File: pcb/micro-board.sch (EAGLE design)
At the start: 122 parts, among them IC1 STM32F401RET6U, IC2 LDS3985M33R, IC3 LDS3985M33R, IC4 HX711, IC5 TLV2462IP, J12 B2B-PH-K-S_LF__SN_, J14 3V3 LED, J15 VDDA LED, J16 HX711 LED, J18 DC Power, J3 Button / ADC Header, Q1 S8550, U1 MCP73831.SOT23-5, U2 BR24S64FJ-WE2, X1 16MHz

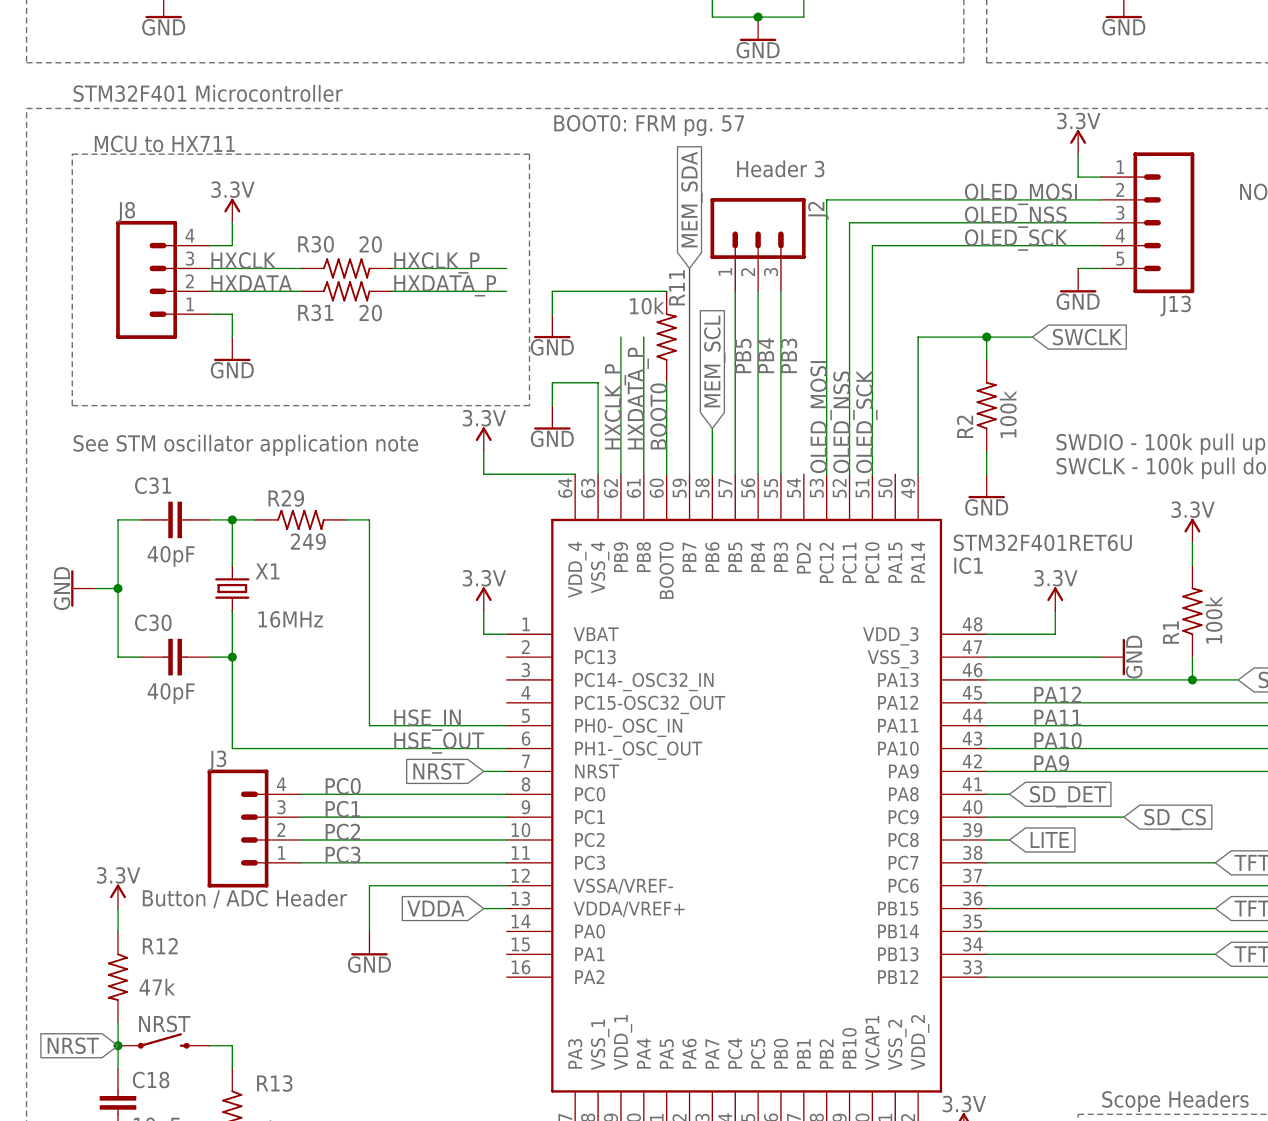
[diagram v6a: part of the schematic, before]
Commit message: Updated the PCB with more silkscreen and ESD protection resistors
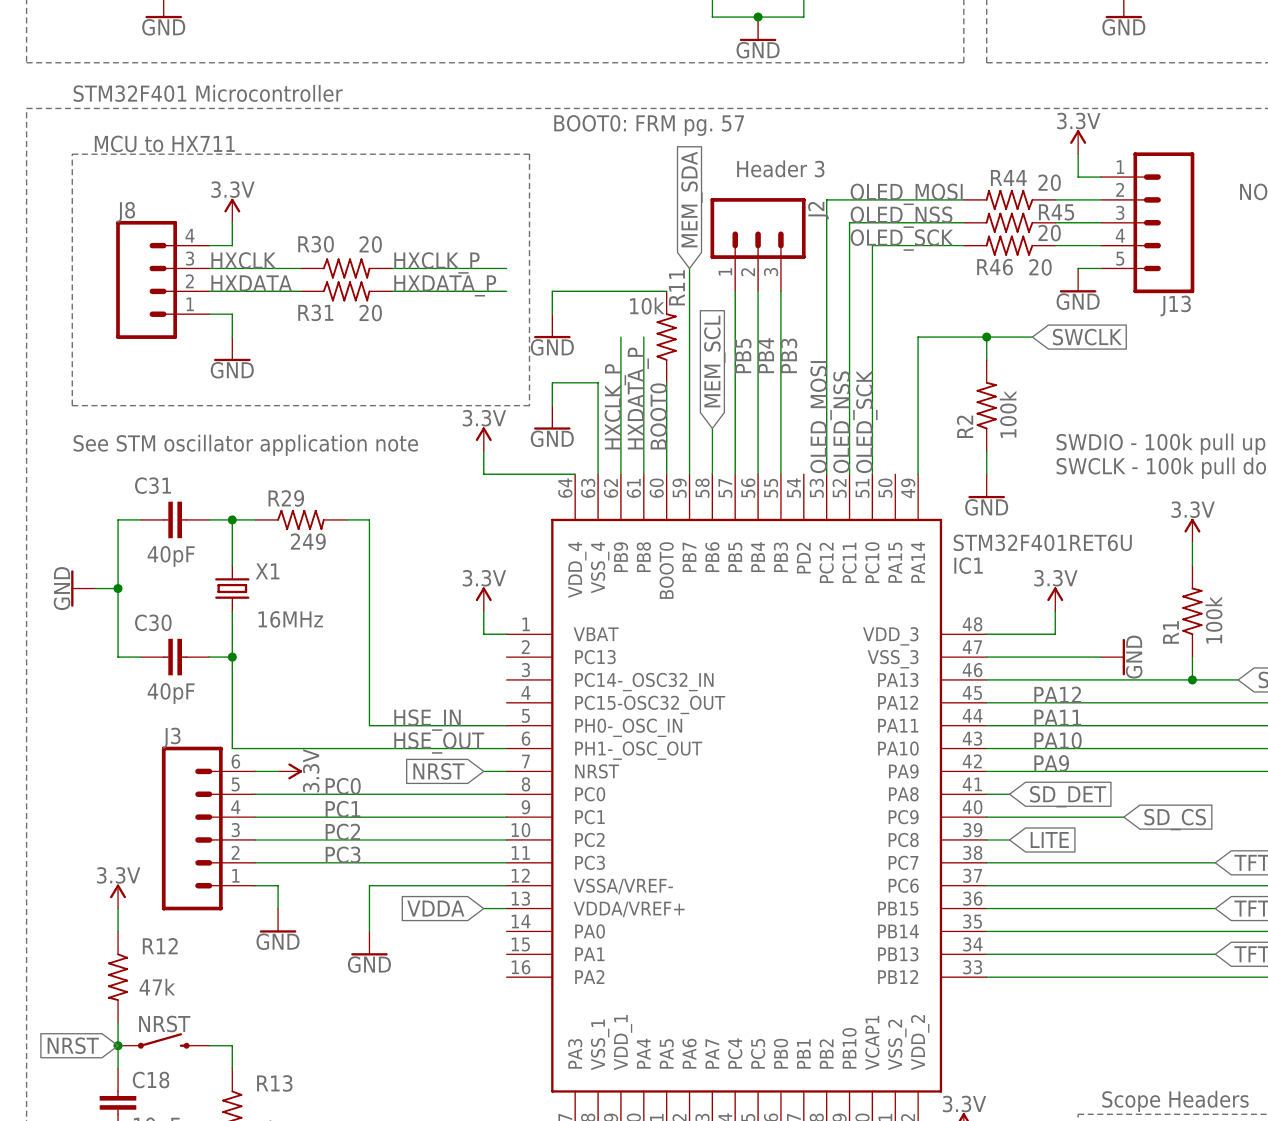
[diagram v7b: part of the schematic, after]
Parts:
- added R44, R45, R46: 20, LinnesLab-Passives:RESISTOR0603
- J3: value Button / ADC Header -> (none); device LinnesLab-Connectors:CONN_04 -> LinnesLab-Connectors:CONN_06LOCK
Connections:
- new net N$20: J13.3, R45.1
- new net N$21: J13.4, R46.1
- new net N$8: J13.2, R44.1
- net 3.3V: now also J3.6
- net GND: now also J3.1
- net OLED_MOSI: now also R44.2; no longer J13.2
- net OLED_NSS: now also R45.2; no longer J13.3
- net OLED_SCK: now also R46.2; no longer J13.4
- net PC0: now also J3.5; no longer J3.4
- net PC1: now also J3.4; no longer J3.3
- net PC2: now also J3.3; no longer J3.2
- net PC3: now also J3.2; no longer J3.1
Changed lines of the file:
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@@
 <setting verticaltext="up"/>
 </settings>
-<grid distance="0.1" unitdist="inch" unit="inch" style="lines" multiple="1" display="yes" altdistance="0.01" altunitdist="inch" altunit="inch"/>
+<grid distance="0.1" unitdist="inch" unit="inch" style="lines" multiple="1" display="no" altdistance="0.01" altunitdist="inch" altunit="inch"/>
 <layers>
 <layer number="1" name="Top" color="4" fill="1" visible="no" active="no"/>
@@
 <part name="GND13" library="LinnesLab-Symbols" deviceset="GND" device=""/>
 <part name="J2" library="LinnesLab-Connectors" deviceset="CONN_03" device=""/>
-<part name="J3" library="LinnesLab-Connectors" deviceset="CONN_04" device="" value="Button / ADC Header"/>
 <part name="GND14" library="LinnesLab-Symbols" deviceset="GND" device=""/>
 <part name="R1" library="LinnesLab-Passives" deviceset="RESISTOR" device="0603" package3d_urn="urn:adsk.eagle:package:15661944/2" value="100k"/>
@@
 <part name="R42" library="LinnesLab-Passives" deviceset="RESISTOR" device="0603" package3d_urn="urn:adsk.eagle:package:15661944/2" value="20"/>
 <part name="R43" library="LinnesLab-Passives" deviceset="RESISTOR" device="0603" package3d_urn="urn:adsk.eagle:package:15661944/2" value="20"/>
+<part name="R44" library="LinnesLab-Passives" deviceset="RESISTOR" device="0603" package3d_urn="urn:adsk.eagle:package:15661944/2" value="20"/>
+<part name="R45" library="LinnesLab-Passives" deviceset="RESISTOR" device="0603" package3d_urn="urn:adsk.eagle:package:15661944/2" value="20"/>
+<part name="R46" library="LinnesLab-Passives" deviceset="RESISTOR" device="0603" package3d_urn="urn:adsk.eagle:package:15661944/2" value="20"/>
+<part name="J3" library="LinnesLab-Connectors" deviceset="CONN_06" device="LOCK"/>
+<part name="GND18" library="LinnesLab-Symbols" deviceset="GND" device=""/>
+<part name="SUPPLY41" library="LinnesLab-Symbols" deviceset="3.3V" device=""/>
 </parts>
 <sheets>
@@
 <attribute name="NAME" x="86.868" y="149.86" size="1.778" layer="95" font="vector" rot="R270"/>
 </instance>
-<instance part="J3" gate="G$1" x="25.4" y="78.74" smashed="yes">
-<attribute name="VALUE" x="12.7" y="71.374" size="1.778" layer="96" font="vector"/>
-<attribute name="NAME" x="20.32" y="86.868" size="1.778" layer="95" font="vector"/>
-</instance>
 <instance part="GND14" gate="G$1" x="58.42" y="124.46" smashed="yes">
 <attribute name="VALUE" x="58.42" y="124.206" size="1.778" layer="96" align="top-center"/>
@@
 <attribute name="VALUE" x="75.946" y="30.734" size="1.778" layer="96" rot="R90"/>
 </instance>
+<instance part="R44" gate="G$1" x="109.22" y="149.86" smashed="yes" rot="R180">
+<attribute name="NAME" x="111.252" y="153.1874" size="1.778" layer="95" rot="R180"/>
+<attribute name="VALUE" x="115.062" y="152.654" size="1.778" layer="96" rot="R180"/>
+</instance>
+<instance part="R45" gate="G$1" x="109.22" y="147.32" smashed="yes" rot="R180">
+<attribute name="NAME" x="116.586" y="149.3774" size="1.778" layer="95" rot="R180"/>
+<attribute name="VALUE" x="115.062" y="147.066" size="1.778" layer="96" rot="R180"/>
+</instance>
+<instance part="R46" gate="G$1" x="109.22" y="144.78" smashed="yes" rot="R180">
+<attribute name="NAME" x="109.728" y="143.2814" size="1.778" layer="95" rot="R180"/>
+<attribute name="VALUE" x="114.046" y="143.256" size="1.778" layer="96" rot="R180"/>
+</instance>
+<instance part="J3" gate="G$1" x="20.32" y="78.74" smashed="yes">
+<attribute name="VALUE" x="15.24" y="68.834" size="1.778" layer="96" font="vector"/>
+<attribute name="NAME" x="15.24" y="89.408" size="1.778" layer="95" font="vector"/>
+</instance>
+<instance part="GND18" gate="G$1" x="27.94" y="68.58" smashed="yes">
+<attribute name="VALUE" x="27.94" y="68.326" size="1.778" layer="96" align="top-center"/>
+</instance>
+<instance part="SUPPLY41" gate="G$1" x="27.94" y="86.36" smashed="yes" rot="R270">
+<attribute name="VALUE" x="30.734" y="86.36" size="1.778" layer="96" rot="R270" align="bottom-center"/>
+</instance>
 </instances>
 <busses>
@@
 <wire x1="182.88" y1="127" x2="187.96" y2="127" width="0.1524" layer="91"/>
 </segment>
+<segment>
+<pinref part="GND18" gate="G$1" pin="GND"/>
+<pinref part="J3" gate="G$1" pin="1"/>
+<wire x1="27.94" y1="71.12" x2="27.94" y2="73.66" width="0.1524" layer="91"/>
+<wire x1="27.94" y1="73.66" x2="25.4" y2="73.66" width="0.1524" layer="91"/>
+</segment>
 </net>
 <net name="N$3" class="0">
@@
 <segment>
 <pinref part="IC1" gate="G$1" pin="PC3"/>
-<pinref part="J3" gate="G$1" pin="1"/>
-<wire x1="53.34" y1="76.2" x2="30.48" y2="76.2" width="0.1524" layer="91"/>
+<wire x1="53.34" y1="76.2" x2="25.4" y2="76.2" width="0.1524" layer="91"/>
 <label x="33.02" y="76.2" size="1.778" layer="95"/>
+<pinref part="J3" gate="G$1" pin="2"/>
 </segment>
 </net>
@@
 <segment>
 <pinref part="IC1" gate="G$1" pin="PC10"/>
-<pinref part="J13" gate="G$1" pin="4"/>
 <wire x1="93.98" y1="119.38" x2="93.98" y2="144.78" width="0.1524" layer="91"/>
-<wire x1="93.98" y1="144.78" x2="119.38" y2="144.78" width="0.1524" layer="91"/>
-<label x="104.14" y="144.78" size="1.778" layer="95"/>
+<label x="91.44" y="144.78" size="1.778" layer="95"/>
 <label x="93.98" y="119.38" size="1.778" layer="95" rot="R90"/>
+<pinref part="R46" gate="G$1" pin="2"/>
+<wire x1="93.98" y1="144.78" x2="104.14" y2="144.78" width="0.1524" layer="91"/>
 </segment>
 </net>
@@
 <pinref part="IC1" gate="G$1" pin="PC11"/>
 <wire x1="91.44" y1="119.38" x2="91.44" y2="147.32" width="0.1524" layer="91"/>
-<pinref part="J13" gate="G$1" pin="3"/>
-<wire x1="91.44" y1="147.32" x2="119.38" y2="147.32" width="0.1524" layer="91"/>
-<label x="104.14" y="147.32" size="1.778" layer="95"/>
+<label x="91.44" y="147.32" size="1.778" layer="95"/>
 <label x="91.44" y="119.38" size="1.778" layer="95" rot="R90"/>
+<pinref part="R45" gate="G$1" pin="2"/>
+<wire x1="91.44" y1="147.32" x2="104.14" y2="147.32" width="0.1524" layer="91"/>
 </segment>
 </net>
@@
 <segment>
 <pinref part="IC1" gate="G$1" pin="PC12"/>
-<pinref part="J13" gate="G$1" pin="2"/>
 <wire x1="88.9" y1="119.38" x2="88.9" y2="149.86" width="0.1524" layer="91"/>
-<wire x1="88.9" y1="149.86" x2="119.38" y2="149.86" width="0.1524" layer="91"/>
-<label x="104.14" y="149.86" size="1.778" layer="95"/>
+<label x="91.44" y="149.86" size="1.778" layer="95"/>
 <label x="88.9" y="119.38" size="1.778" layer="95" rot="R90"/>
+<pinref part="R44" gate="G$1" pin="2"/>
+<wire x1="88.9" y1="149.86" x2="104.14" y2="149.86" width="0.1524" layer="91"/>
 </segment>
 </net>
@@
 <pinref part="SUPPLY40" gate="G$1" pin="3.3V"/>
 </segment>
+<segment>
+<pinref part="SUPPLY41" gate="G$1" pin="3.3V"/>
+<pinref part="J3" gate="G$1" pin="6"/>
+<wire x1="27.94" y1="86.36" x2="25.4" y2="86.36" width="0.1524" layer="91"/>
+</segment>
 </net>
 <net name="HX_SDA" class="0">
@@
 <net name="PC0" class="0">
 <segment>
-<pinref part="J3" gate="G$1" pin="4"/>
 <pinref part="IC1" gate="G$1" pin="PC0"/>
-<wire x1="30.48" y1="83.82" x2="53.34" y2="83.82" width="0.1524" layer="91"/>
+<wire x1="25.4" y1="83.82" x2="53.34" y2="83.82" width="0.1524" layer="91"/>
 <label x="33.02" y="83.82" size="1.778" layer="95"/>
+<pinref part="J3" gate="G$1" pin="5"/>
 </segment>
 </net>
@@
 <segment>
 <pinref part="IC1" gate="G$1" pin="PC1"/>
-<pinref part="J3" gate="G$1" pin="3"/>
-<wire x1="53.34" y1="81.28" x2="30.48" y2="81.28" width="0.1524" layer="91"/>
+<wire x1="53.34" y1="81.28" x2="25.4" y2="81.28" width="0.1524" layer="91"/>
 <label x="33.02" y="81.28" size="1.778" layer="95"/>
+<pinref part="J3" gate="G$1" pin="4"/>
 </segment>
 </net>
 <net name="PC2" class="0">
 <segment>
-<pinref part="J3" gate="G$1" pin="2"/>
 <pinref part="IC1" gate="G$1" pin="PC2"/>
-<wire x1="30.48" y1="78.74" x2="53.34" y2="78.74" width="0.1524" layer="91"/>
+<wire x1="25.4" y1="78.74" x2="53.34" y2="78.74" width="0.1524" layer="91"/>
 <label x="33.02" y="78.74" size="1.778" layer="95"/>
+<pinref part="J3" gate="G$1" pin="3"/>
 </segment>
 </net>
@@
 </segment>
 </net>
+<net name="N$8" class="0">
+<segment>
+<pinref part="R44" gate="G$1" pin="1"/>
+<pinref part="J13" gate="G$1" pin="2"/>
+<wire x1="114.3" y1="149.86" x2="119.38" y2="149.86" width="0.1524" layer="91"/>
+</segment>
+</net>
+<net name="N$20" class="0">
+<segment>
+<pinref part="J13" gate="G$1" pin="3"/>
+<pinref part="R45" gate="G$1" pin="1"/>
+<wire x1="119.38" y1="147.32" x2="114.3" y2="147.32" width="0.1524" layer="91"/>
+</segment>
+</net>
+<net name="N$21" class="0">
+<segment>
+<pinref part="R46" gate="G$1" pin="1"/>
+<pinref part="J13" gate="G$1" pin="4"/>
+<wire x1="114.3" y1="144.78" x2="119.38" y2="144.78" width="0.1524" layer="91"/>
+</segment>
+</net>
